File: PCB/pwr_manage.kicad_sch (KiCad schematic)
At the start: 0 parts

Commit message: [Schem] Added sensors connectors & finished Step down circuit
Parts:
- added C26, C29: 10 uF, symbol Device:C
- added C27, C28: 22 uF, symbol Device:C
- added C31, C34: 130 pF, symbol Device:C
- added C32, C33: 220 pF, symbol Device:C
- added D8, D9: SS34, Diode_SMD:D_SMA, symbol Diode:SS34
- added J18: 12v 20Ah Battery, symbol Connector:Screw_Terminal_01x02
- added L1, L2: 4.7 uH, symbol Device:L
- added R60, R67: 68k, symbol Device:R
- added R61, R69: 200k, symbol Device:R
- added R62, R65: 45k, symbol Device:R
- added R63, R66: 8.2k, symbol Device:R
- added R64, R68: 1k, symbol Device:R
- added U13, U14: MP1584EN-LF-Z, SOIC8E_MPS, symbol WALL-E_symbols:MP1584EN-LF-Z
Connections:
- new net: C31.2, D8.1 (K), L1.2, U13.1 (SW)
- new net: R64.2, U13.2 (EN)
- new net: C32.1, U13.3 (COMP)
- new net: R62.2, R63.1, U13.4 (FB)
- new net: R61.2, U13.6 (FREQ)
- new net: C31.1, U13.8 (BST)
- new net: C32.2, R60.1
- new net: R68.2, U14.2 (EN)
- new net: R65.2, R66.1, U14.4 (FB)
- new net: C34.2, D9.1 (K), L2.2, U14.1 (SW)
- new net: C33.1, U14.3 (COMP)
- new net: C33.2, R67.1
- new net: C34.1, U14.8 (BST)
- new net: R69.2, U14.6 (FREQ)
- new net +12V: C26.1, C29.1, J18.1 (Pin_1), U13.7 (VIN), U14.7 (VIN)
- new net +5V: C27.2, L1.1, R62.1
- new net +5VA: C28.2, L2.1, R65.1
- new net GND: C26.2, C27.1, C28.1, C29.2, D8.2 (A), D9.2 (A), J18.2 (Pin_2), R60.2, R61.1, R63.2, R64.1, R66.2, R67.2, R68.1, R69.1, U13.5 (GND), U13.EPAD, U14.5 (GND), U14.EPAD
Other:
- note added: "Logic V"
- note added: "Servos V"

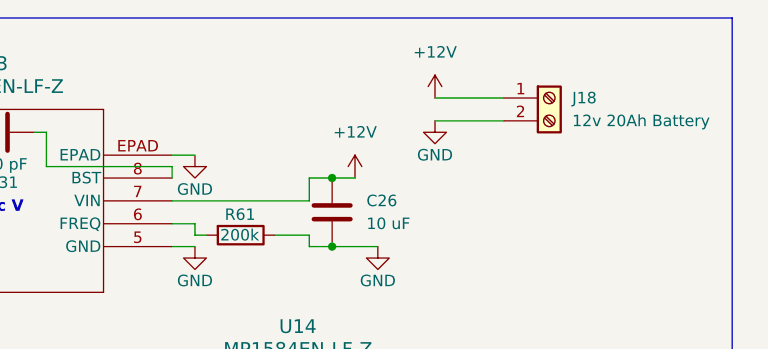
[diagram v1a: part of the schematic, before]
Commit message: [Schem] Finished the Hierarchy Labels of all the pages
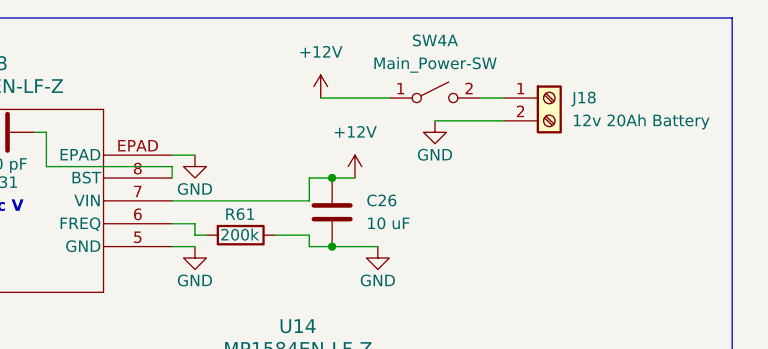
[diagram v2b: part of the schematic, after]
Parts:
- added SW4: Main_Power-SW, symbol Switch:SW_DPST_x2
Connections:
- net +12V: now also SW4.1 (A); no longer J18.1 (Pin_1)
- new net: J18.1 (Pin_1), SW4.2 (B)
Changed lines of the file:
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@@
 	(wire
 		(pts
-			(xy 191.77 67.31) (xy 199.39 67.31)
-		)
-		(stroke
-			(width 0)
-			(type default)
-		)
-	)
-	(wire
-		(pts
 			(xy 177.8 83.82) (xy 180.34 83.82)
 		)
@@
 	(wire
 		(pts
+			(xy 179.07 67.31) (xy 186.69 67.31)
+		)
+		(stroke
+			(width 0)
+			(type default)
+		)
+	)
+	(wire
+		(pts
 			(xy 113.03 73.66) (xy 121.92 73.66)
 		)
@@
 		)
 	)
+	(wire
+		(pts
+			(xy 196.85 67.31) (xy 199.39 67.31)
+		)
+		(stroke
+			(width 0)
+			(type default)
+		)
+	)
 	(symbol
 		(lib_id "power:GND")
@@
 	)
 	(symbol
+		(lib_id "Switch:SW_DPST_x2")
+		(at 191.77 67.31 0)
+		(unit 1)
+		(body_style 1)
+		(exclude_from_sim no)
+		(in_bom yes)
+		(on_board yes)
+		(in_pos_files yes)
+		(dnp no)
+		(fields_autoplaced yes)
+		(property "Reference" "SW4"
+			(at 191.77 60.96 0)
+			(show_name no)
+			(do_not_autoplace no)
+			(effects
+				(font
+					(size 1.27 1.27)
+				)
+			)
+		)
+		(property "Value" "Main_Power-SW"
+			(at 191.77 63.5 0)
+			(show_name no)
+			(do_not_autoplace no)
+			(effects
+				(font
+					(size 1.27 1.27)
+				)
+			)
+		)
+		(property "Footprint" ""
+			(at 191.77 67.31 0)
+			(hide yes)
+			(show_name no)
+			(do_not_autoplace no)
+			(effects
+				(font
+					(size 1.27 1.27)
+				)
+			)
+		)
+		(property "Datasheet" ""
+			(at 191.77 67.31 0)
+			(hide yes)
+			(show_name no)
+			(do_not_autoplace no)
+			(effects
+				(font
+					(size 1.27 1.27)
+				)
+			)
+		)
+		(property "Description" "Single Pole Single Throw (SPST) switch, separate symbol"
+			(at 191.77 67.31 0)
+			(hide yes)
+			(show_name no)
+			(do_not_autoplace no)
+			(effects
+				(font
+					(size 1.27 1.27)
+				)
+			)
+		)
+		(pin "1"
+		)
+		(pin "2"
+		)
+		(pin "3"
+		)
+		(pin "4"
+		)
+		(instances
+			(project "PCB"
+				(path "/ce714510-8789-438c-9780-97c7c26e78af/cf1faa47-3100-4a18-98c2-24423d277f27"
+					(reference "SW4")
+					(unit 1)
+				)
+			)
+		)
+	)
+	(symbol
 		(lib_id "WALL-E_symbols:MP1584EN-LF-Z")
 		(at 121.92 73.66 0)
@@
 	(symbol
 		(lib_id "power:+12V")
-		(at 191.77 67.31 0)
+		(at 179.07 67.31 0)
 		(unit 1)
 		(body_style 1)
@@
 		(fields_autoplaced yes)
 		(property "Reference" "#PWR0105"
-			(at 191.77 71.12 0)
+			(at 179.07 71.12 0)
 			(hide yes)
 			(show_name no)
@@
 		)
 		(property "Value" "+12V"
-			(at 191.77 62.23 0)
+			(at 179.07 62.23 0)
 			(show_name no)
 			(do_not_autoplace no)
@@
 		)
 		(property "Footprint" ""
-			(at 191.77 67.31 0)
+			(at 179.07 67.31 0)
 			(hide yes)
 			(show_name no)
@@
 		)
 		(property "Datasheet" ""
-			(at 191.77 67.31 0)
+			(at 179.07 67.31 0)
 			(hide yes)
 			(show_name no)
@@
 		)
 		(property "Description" "Power symbol creates a global label with name \"+12V\""
-			(at 191.77 67.31 0)
+			(at 179.07 67.31 0)
 			(hide yes)
 			(show_name no)

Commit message: [PCB] Assigned all the footprints
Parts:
- C26, C27, C28, C29, C31, C32, C33, C34: footprint (none) -> Capacitor_SMD:C_0603_1608Metric_Pad1.08x0.95mm_HandSolder
- J18: footprint (none) -> Connector_BarrelJack:BarrelJack_Horizontal
- L1, L2: footprint (none) -> Inductor_SMD:L_0603_1608Metric_Pad1.05x0.95mm_HandSolder
- R60, R61, R62, R63, R64, R65, R66, R67, R68, R69: footprint (none) -> Resistor_SMD:R_0603_1608Metric_Pad0.98x0.95mm_HandSolder
- SW4: footprint (none) -> Package_SO:TSSOP-20_4.4x6.5mm_P0.65mm
- U13, U14: footprint SOIC8E_MPS -> Package_SO:SOIC-8-1EP_3.9x4.9mm_P1.27mm_EP2.29x3mm_ThermalVias
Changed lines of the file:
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@@
 			)
 		)
-		(property "Footprint" ""
+		(property "Footprint" "Inductor_SMD:L_0603_1608Metric_Pad1.05x0.95mm_HandSolder"
 			(at 101.6 73.66 0)
 			(hide yes)
@@
 			)
 		)
-		(property "Footprint" ""
+		(property "Footprint" "Package_SO:TSSOP-20_4.4x6.5mm_P0.65mm"
 			(at 191.77 67.31 0)
 			(hide yes)
@@
 			)
 		)
-		(property "Footprint" "SOIC8E_MPS"
+		(property "Footprint" "Package_SO:SOIC-8-1EP_3.9x4.9mm_P1.27mm_EP2.29x3mm_ThermalVias"
 			(at 121.92 73.66 0)
 			(hide yes)
@@
 			)
 		)
-		(property "Footprint" ""
+		(property "Footprint" "Capacitor_SMD:C_0603_1608Metric_Pad1.08x0.95mm_HandSolder"
 			(at 106.3752 96.52 0)
 			(hide yes)
@@
 			)
 		)
-		(property "Footprint" ""
+		(property "Footprint" "Resistor_SMD:R_0603_1608Metric_Pad0.98x0.95mm_HandSolder"
 			(at 148.59 107.188 90)
 			(hide yes)
@@
 			)
 		)
-		(property "Footprint" ""
+		(property "Footprint" "Resistor_SMD:R_0603_1608Metric_Pad0.98x0.95mm_HandSolder"
 			(at 129.032 119.38 90)
 			(hide yes)
@@
 			)
 		)
-		(property "Footprint" ""
+		(property "Footprint" "Resistor_SMD:R_0603_1608Metric_Pad0.98x0.95mm_HandSolder"
 			(at 94.742 78.74 90)
 			(hide yes)
@@
 			)
 		)
-		(property "Footprint" ""
+		(property "Footprint" "Capacitor_SMD:C_0603_1608Metric_Pad1.08x0.95mm_HandSolder"
 			(at 215.5952 113.03 0)
 			(hide yes)
@@
 			)
 		)
-		(property "Footprint" ""
+		(property "Footprint" "Inductor_SMD:L_0603_1608Metric_Pad1.05x0.95mm_HandSolder"
 			(at 135.89 102.87 0)
 			(hide yes)
@@
 			)
 		)
-		(property "Footprint" ""
+		(property "Footprint" "Capacitor_SMD:C_0603_1608Metric_Pad1.08x0.95mm_HandSolder"
 			(at 155.9052 120.65 0)
 			(hide yes)
@@
 			)
 		)
-		(property "Footprint" ""
+		(property "Footprint" "Capacitor_SMD:C_0603_1608Metric_Pad1.08x0.95mm_HandSolder"
 			(at 91.44 72.6948 0)
 			(hide yes)
@@
 			)
 		)
-		(property "Footprint" ""
+		(property "Footprint" "Capacitor_SMD:C_0603_1608Metric_Pad1.08x0.95mm_HandSolder"
 			(at 139.7 72.0852 0)
 			(hide yes)
@@
 			)
 		)
-		(property "Footprint" ""
+		(property "Footprint" "Capacitor_SMD:C_0603_1608Metric_Pad1.08x0.95mm_HandSolder"
 			(at 173.99 101.2952 0)
 			(hide yes)
@@
 			)
 		)
-		(property "Footprint" ""
+		(property "Footprint" "Resistor_SMD:R_0603_1608Metric_Pad0.98x0.95mm_HandSolder"
 			(at 170.18 80.772 90)
 			(hide yes)
@@
 			)
 		)
-		(property "Footprint" ""
+		(property "Footprint" "Capacitor_SMD:C_0603_1608Metric_Pad1.08x0.95mm_HandSolder"
 			(at 181.3052 83.82 0)
 			(hide yes)
@@
 			)
 		)
-		(property "Footprint" ""
+		(property "Footprint" "Connector_BarrelJack:BarrelJack_Horizontal"
 			(at 204.47 67.31 0)
 			(hide yes)
@@
 			)
 		)
-		(property "Footprint" ""
+		(property "Footprint" "Resistor_SMD:R_0603_1608Metric_Pad0.98x0.95mm_HandSolder"
 			(at 94.742 90.17 90)
 			(hide yes)
@@
 			)
 		)
-		(property "Footprint" "SOIC8E_MPS"
+		(property "Footprint" "Package_SO:SOIC-8-1EP_3.9x4.9mm_P1.27mm_EP2.29x3mm_ThermalVias"
 			(at 156.21 102.87 0)
 			(hide yes)
@@
 			)
 		)
-		(property "Footprint" ""
+		(property "Footprint" "Resistor_SMD:R_0603_1608Metric_Pad0.98x0.95mm_HandSolder"
 			(at 129.032 107.95 90)
 			(hide yes)
@@
 			)
 		)
-		(property "Footprint" ""
+		(property "Footprint" "Resistor_SMD:R_0603_1608Metric_Pad0.98x0.95mm_HandSolder"
 			(at 103.632 101.6 90)
 			(hide yes)
@@
 			)
 		)
-		(property "Footprint" ""
+		(property "Footprint" "Resistor_SMD:R_0603_1608Metric_Pad0.98x0.95mm_HandSolder"
 			(at 114.3 77.978 90)
 			(hide yes)
@@
 			)
 		)
-		(property "Footprint" ""
+		(property "Footprint" "Resistor_SMD:R_0603_1608Metric_Pad0.98x0.95mm_HandSolder"
 			(at 204.47 109.982 90)
 			(hide yes)
@@
 			)
 		)
-		(property "Footprint" ""
+		(property "Footprint" "Resistor_SMD:R_0603_1608Metric_Pad0.98x0.95mm_HandSolder"
 			(at 153.162 125.73 90)
 			(hide yes)
@@
 			)
 		)
-		(property "Footprint" ""
+		(property "Footprint" "Capacitor_SMD:C_0603_1608Metric_Pad1.08x0.95mm_HandSolder"
 			(at 125.73 101.9048 0)
 			(hide yes)

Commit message: [PCB] Traced the ESP's Type C
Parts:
- SW4: footprint Package_SO:TSSOP-20_4.4x6.5mm_P0.65mm -> Connector_JST:JST_PH_B2B-PH-K_1x02_P2.00mm_Vertical
- U13, U14: footprint Package_SO:SOIC-8-1EP_3.9x4.9mm_P1.27mm_EP2.29x3mm_ThermalVias -> Wall_E_FPs:SOIC12
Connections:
- net GND: now also U13.9 (EPAD), U14.9 (EPAD); no longer U13.EPAD, U14.EPAD
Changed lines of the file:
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@@
 			)
 		)
-		(property "Footprint" "Package_SO:TSSOP-20_4.4x6.5mm_P0.65mm"
+		(property "Footprint" "Connector_JST:JST_PH_B2B-PH-K_1x02_P2.00mm_Vertical"
 			(at 191.77 67.31 0)
 			(hide yes)
@@
 	)
 	(symbol
+		(lib_name "MP1584EN-LF-Z_1")
 		(lib_id "WALL-E_symbols:MP1584EN-LF-Z")
 		(at 121.92 73.66 0)
@@
 			)
 		)
-		(property "Footprint" "Package_SO:SOIC-8-1EP_3.9x4.9mm_P1.27mm_EP2.29x3mm_ThermalVias"
+		(property "Footprint" "Wall_E_FPs:SOIC12"
 			(at 121.92 73.66 0)
 			(hide yes)
@@
 		(pin "6"
 		)
-		(pin "EPAD"
+		(pin "9"
 		)
 		(pin "5"
@@
 			)
 		)
-		(property "Footprint" "Package_SO:SOIC-8-1EP_3.9x4.9mm_P1.27mm_EP2.29x3mm_ThermalVias"
+		(property "Footprint" "Wall_E_FPs:SOIC12"
 			(at 156.21 102.87 0)
 			(hide yes)
@@
 		(pin "6"
 		)
-		(pin "EPAD"
+		(pin "9"
 		)
 		(pin "5"

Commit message: [PCB] Splited the PCB into two boards
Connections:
- net +5V renamed +5VCo
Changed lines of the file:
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@@
 		(in_pos_files yes)
 		(dnp no)
-		(fields_autoplaced yes)
 		(property "Reference" "#PWR091"
 			(at 92.71 74.93 0)
@@
 			)
 		)
-		(property "Value" "+5V"
-			(at 92.71 66.04 0)
+		(property "Value" "+5VCo"
+			(at 91.186 66.04 0)
 			(show_name no)
 			(do_not_autoplace no)
@@
 					(size 1.27 1.27)
 				)
+				(justify left)
 			)
 		)
